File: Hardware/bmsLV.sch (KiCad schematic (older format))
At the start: 30 parts, among them J1 Conn_01x06_Male, J2 USB_B_Mini, K1 RM85V7, Q1 BSS138, SW1 SW_Push, U1 STM32F103C8Tx, Y1 Crystal

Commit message: Going back to work
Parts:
- added D16: D_Small, Diode_SMD:D_SMB, symbol Device:D_Small
- added J13: Conn_01x04_Male, Connector_PinHeader_2.54mm:PinHeader_1x04_P2.54mm_Vertical, symbol Connector:Conn_01x04_Male
- added R39, R40: 27, Resistor_SMD:R_1206_3216Metric, symbol Device:R_Small
- K1: footprint RM85V7:RM85V7-Z-24VDC -> RM85V7:RM85V7
- R1, R2, R3, R4: value 1K -> 120
- gave numbers to parts that had none: 2
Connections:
- net +24V: now also D16.1 (K)
- net +5V: now also J13.1 (Pin_1)
- net GND: now also J13.4 (Pin_4)
- net USB_DM: now also J13.2 (Pin_2), R39.1; no longer U1.32 (PA11)
- net USB_DP: now also J13.3 (Pin_3), R40.1; no longer U1.33 (PA12)
- net at K1.2 (A2), Q1.3 (D): now also D16.2 (A)
- new net: R39.2, U1.32 (PA11)
- new net: R40.2, U1.33 (PA12)
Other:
- moved on the sheet: J2
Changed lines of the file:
@@
 P 3400 4250
 F 0 "R2" V 3204 4250 50  0000 C CNN
-F 1 "1K" V 3295 4250 50  0000 C CNN
+F 1 "120" V 3295 4250 50  0000 C CNN
 F 2 "Resistor_SMD:R_1206_3216Metric" H 3400 4250 50  0001 C CNN
 F 3 "~" H 3400 4250 50  0001 C CNN
@@
 P 3400 5050
 F 0 "R3" V 3204 5050 50  0000 C CNN
-F 1 "1K" V 3295 5050 50  0000 C CNN
+F 1 "120" V 3295 5050 50  0000 C CNN
 F 2 "Resistor_SMD:R_1206_3216Metric" H 3400 5050 50  0001 C CNN
 F 3 "~" H 3400 5050 50  0001 C CNN
@@
 P 3400 5150
 F 0 "R4" V 3204 5150 50  0000 C CNN
-F 1 "1K" V 3295 5150 50  0000 C CNN
+F 1 "120" V 3295 5150 50  0000 C CNN
 F 2 "Resistor_SMD:R_1206_3216Metric" H 3400 5150 50  0001 C CNN
 F 3 "~" H 3400 5150 50  0001 C CNN
@@
 P 3400 4150
 F 0 "R1" V 3204 4150 50  0000 C CNN
-F 1 "1K" V 3295 4150 50  0000 C CNN
+F 1 "120" V 3295 4150 50  0000 C CNN
 F 2 "Resistor_SMD:R_1206_3216Metric" H 3400 4150 50  0001 C CNN
 F 3 "~" H 3400 4150 50  0001 C CNN
@@
 Wire Wire Line
 	3300 4250 3050 4250
-Text GLabel 5500 5250 2    50   Input ~ 0
+Text GLabel 6100 5250 2    50   Input ~ 0
 USB_DP
-Text GLabel 5500 5150 2    50   Input ~ 0
+Text GLabel 6100 5150 2    50   Input ~ 0
 USB_DM
 $Comp
 L Connector:USB_B_Mini J2
 U 1 1 5FFA0FD0
-P 8150 1550
-F 0 "J2" H 7920 1447 50  0000 R CNN
-F 1 "USB_B_Mini" H 7920 1538 50  0000 R CNN
-F 2 "Connector_USB:USB_Micro-B_Molex_47346-0001" H 8300 1500 50  0001 C CNN
-F 3 "~" H 8300 1500 50  0001 C CNN
-	1    8150 1550
+P 8450 1550
+F 0 "J2" H 8220 1447 50  0000 R CNN
+F 1 "USB_B_Mini" H 8220 1538 50  0000 R CNN
+F 2 "Connector_USB:USB_Micro-B_Molex_47346-0001" H 8600 1500 50  0001 C CNN
+F 3 "~" H 8600 1500 50  0001 C CNN
+	1    8450 1550
 	-1   0    0    1
 $EndComp
@@
 L power:GND #PWR019
 U 1 1 5FFA2879
-P 8450 1100
-F 0 "#PWR019" H 8450 850 50  0001 C CNN
-F 1 "GND" H 8455 927 50  0000 C CNN
-F 2 "" H 8450 1100 50  0001 C CNN
-F 3 "" H 8450 1100 50  0001 C CNN
-	1    8450 1100
-	1    0    0    -1
-$EndComp
-Wire Wire Line
-	8150 1100 8150 1150
+P 8750 1100
+F 0 "#PWR019" H 8750 850 50  0001 C CNN
+F 1 "GND" H 8755 927 50  0000 C CNN
+F 2 "" H 8750 1100 50  0001 C CNN
+F 3 "" H 8750 1100 50  0001 C CNN
+	1    8750 1100
+	1    0    0    -1
+$EndComp
+Wire Wire Line
+	8450 1100 8450 1150
 $Comp
 L power:+5V #PWR014
 U 1 1 5FFAAF0D
-P 7450 1750
-F 0 "#PWR014" H 7450 1600 50  0001 C CNN
-F 1 "+5V" H 7465 1923 50  0000 C CNN
-F 2 "" H 7450 1750 50  0001 C CNN
-F 3 "" H 7450 1750 50  0001 C CNN
-	1    7450 1750
-	1    0    0    -1
-$EndComp
-Wire Wire Line
-	8150 1100 8250 1100
-Wire Wire Line
-	8250 1150 8250 1100
-Connection ~ 8250 1100
-Wire Wire Line
-	8250 1100 8450 1100
-Text GLabel 7850 1450 0    50   Input ~ 0
+P 7750 1750
+F 0 "#PWR014" H 7750 1600 50  0001 C CNN
+F 1 "+5V" H 7765 1923 50  0000 C CNN
+F 2 "" H 7750 1750 50  0001 C CNN
+F 3 "" H 7750 1750 50  0001 C CNN
+	1    7750 1750
+	1    0    0    -1
+$EndComp
+Wire Wire Line
+	8450 1100 8550 1100
+Wire Wire Line
+	8550 1150 8550 1100
+Connection ~ 8550 1100
+Wire Wire Line
+	8550 1100 8750 1100
+Text GLabel 8150 1450 0    50   Input ~ 0
 USB_DM
-Text GLabel 7850 1550 0    50   Input ~ 0
+Text GLabel 8150 1550 0    50   Input ~ 0
 USB_DP
 Wire Wire Line
-	7450 1750 7850 1750
+	7750 1750 8150 1750
 $Comp
 L power:+3.3V #PWR03
@@
 P 7900 2450
 AR Path="/5FAD7AC5/5FFFFAC2" Ref="J?"  Part="1"
-AR Path="/5FFFFAC2" Ref="J?"  Part="1"
-F 0 "J?" H 7792 2125 50  0000 C CNN
+AR Path="/5FFFFAC2" Ref="J3"  Part="1"
+F 0 "J3" H 7792 2125 50  0000 C CNN
 F 1 "Conn_01x02_Female" H 7792 2216 50  0000 C CNN
 F 2 "TerminalBlock:TerminalBlock_bornier-2_P5.08mm" H 7900 2450 50  0001 C CNN
@@
 P 8250 2450
 AR Path="/5FAD7AC5/5FFFFAC8" Ref="#PWR?"  Part="1"
-AR Path="/5FFFFAC8" Ref="#PWR?"  Part="1"
-F 0 "#PWR?" H 8250 2200 50  0001 C CNN
+AR Path="/5FFFFAC8" Ref="#PWR0101"  Part="1"
+F 0 "#PWR0101" H 8250 2200 50  0001 C CNN
 F 1 "GND" H 8255 2277 50  0000 C CNN
 F 2 "" H 8250 2450 50  0001 C CNN
@@
 	8250 2350 8250 2300
 $Comp
-L power:VCC #PWR?
+L power:VCC #PWR0102
 U 1 1 60004D86
 P 8250 2300
-F 0 "#PWR?" H 8250 2150 50  0001 C CNN
+F 0 "#PWR0102" H 8250 2150 50  0001 C CNN
 F 1 "VCC" H 8267 2473 50  0000 C CNN
 F 2 "" H 8250 2300 50  0001 C CNN
@@
 P 7900 3000
 AR Path="/5FB83FF2/60009E9A" Ref="J?"  Part="1"
-AR Path="/60009E9A" Ref="J?"  Part="1"
-F 0 "J?" H 7928 2976 50  0000 L CNN
+AR Path="/60009E9A" Ref="J5"  Part="1"
+F 0 "J5" H 7928 2976 50  0000 L CNN
 F 1 "Conn_01x02_Female" H 7928 2885 50  0000 L CNN
 F 2 "TerminalBlock:TerminalBlock_bornier-2_P5.08mm" H 7900 3000 50  0001 C CNN
@@
 F 0 "K1" H 8375 5475 50  0000 C CNN
 F 1 "RM85V7" H 8375 5384 50  0000 C CNN
-F 2 "RM85V7:RM85V7-Z-24VDC" V 8500 5200 50  0001 C CNN
+F 2 "RM85V7:RM85V7" V 8500 5200 50  0001 C CNN
 F 3 "" V 8500 5200 50  0001 C CNN
 	1    8350 5200
@@
 Wire Wire Line
 	8000 5350 8000 5600
+$Comp
+L power:GND #PWR018
+U 1 1 6065B29C
+P 8000 6100
+F 0 "#PWR018" H 8000 5850 50  0001 C CNN
+F 1 "GND" H 8005 5927 50  0000 C CNN
+F 2 "" H 8000 6100 50  0001 C CNN
+F 3 "" H 8000 6100 50  0001 C CNN
+	1    8000 6100
+	1    0    0    -1
+$EndComp
+Wire Wire Line
+	7700 5800 7550 5800
+Wire Wire Line
+	7550 5800 7550 6050
+Wire Wire Line
+	7550 6050 7650 6050
+$Comp
+L Device:R_Small R8
+U 1 1 6065E7D3
+P 7750 6050
+F 0 "R8" V 7554 6050 50  0000 C CNN
+F 1 "10K" V 7645 6050 50  0000 C CNN
+F 2 "Resistor_SMD:R_1206_3216Metric" H 7750 6050 50  0001 C CNN
+F 3 "~" H 7750 6050 50  0001 C CNN
+	1    7750 6050
+	0    1    1    0
+$EndComp
+Wire Wire Line
+	8000 6000 8000 6050
+Wire Wire Line
+	8000 6050 7850 6050
+Connection ~ 8000 6050
+Wire Wire Line
+	8000 6050 8000 6100
+Wire Wire Line
+	7550 5800 7450 5800
+Connection ~ 7550 5800
+$Comp
+L Device:R_Small R7
+U 1 1 6066752D
+P 7350 5800
+F 0 "R7" V 7154 5800 50  0000 C CNN
+F 1 "100" V 7245 5800 50  0000 C CNN
+F 2 "Resistor_SMD:R_1206_3216Metric" H 7350 5800 50  0001 C CNN
+F 3 "~" H 7350 5800 50  0001 C CNN
+	1    7350 5800
+	0    1    1    0
+$EndComp
+Wire Wire Line
+	7250 5800 7150 5800
+Wire Wire Line
+	8750 5200 8850 5200
+Wire Wire Line
+	8750 5300 8850 5300
+Text GLabel 8850 5300 2    50   Input ~ 0
+V_Out
+$Comp
+L power:+24V #PWR020
+U 1 1 6068138D
+P 8850 5200
+F 0 "#PWR020" H 8850 5050 50  0001 C CNN
+F 1 "+24V" V 8865 5328 50  0000 L CNN
+F 2 "" H 8850 5200 50  0001 C CNN
+F 3 "" H 8850 5200 50  0001 C CNN
+	1    8850 5200
+	1    0    0    -1
+$EndComp
+Wire Wire Line
+	8000 5350 7900 5350
+Wire Wire Line
+	7900 5150 8000 5150
+Connection ~ 8000 5350
+Connection ~ 8000 5150
+$Comp
+L Device:D_Small D16
+U 1 1 60308393
+P 7900 5250
+F 0 "D16" H 7900 5455 50  0000 C CNN
+F 1 "D_Small" H 7900 5364 50  0000 C CNN
+F 2 "Diode_SMD:D_SMB" V 7900 5250 50  0001 C CNN
+F 3 "~" V 7900 5250 50  0001 C CNN
+	1    7900 5250
+	0    1    1    0
+$EndComp
 $Comp
 L Transistor_FET:BSS138 Q1
@@
 $EndComp
 $Comp
-L power:GND #PWR018
-U 1 1 6065B29C
-P 8000 6100
-F 0 "#PWR018" H 8000 5850 50  0001 C CNN
-F 1 "GND" H 8005 5927 50  0000 C CNN
-F 2 "" H 8000 6100 50  0001 C CNN
-F 3 "" H 8000 6100 50  0001 C CNN
-	1    8000 6100
-	1    0    0    -1
-$EndComp
-Wire Wire Line
-	7700 5800 7550 5800
-Wire Wire Line
-	7550 5800 7550 6050
-Wire Wire Line
-	7550 6050 7650 6050
-$Comp
-L Device:R_Small R8
-U 1 1 6065E7D3
-P 7750 6050
-F 0 "R8" V 7554 6050 50  0000 C CNN
-F 1 "10K" V 7645 6050 50  0000 C CNN
-F 2 "Resistor_SMD:R_1206_3216Metric" H 7750 6050 50  0001 C CNN
-F 3 "~" H 7750 6050 50  0001 C CNN
-	1    7750 6050
-	0    1    1    0
-$EndComp
-Wire Wire Line
-	8000 6000 8000 6050
-Wire Wire Line
-	8000 6050 7850 6050
-Connection ~ 8000 6050
-Wire Wire Line
-	8000 6050 8000 6100
-Wire Wire Line
-	7550 5800 7450 5800
-Connection ~ 7550 5800
-$Comp
-L Device:R_Small R7
-U 1 1 6066752D
-P 7350 5800
-F 0 "R7" V 7154 5800 50  0000 C CNN
-F 1 "100" V 7245 5800 50  0000 C CNN
-F 2 "Resistor_SMD:R_1206_3216Metric" H 7350 5800 50  0001 C CNN
-F 3 "~" H 7350 5800 50  0001 C CNN
-	1    7350 5800
-	0    1    1    0
-$EndComp
-Wire Wire Line
-	7250 5800 7150 5800
-Wire Wire Line
-	8750 5200 8850 5200
-Wire Wire Line
-	8750 5300 8850 5300
-Text GLabel 8850 5300 2    50   Input ~ 0
-V_Out
-$Comp
-L power:+24V #PWR020
-U 1 1 6068138D
-P 8850 5200
-F 0 "#PWR020" H 8850 5050 50  0001 C CNN
-F 1 "+24V" V 8865 5328 50  0000 L CNN
-F 2 "" H 8850 5200 50  0001 C CNN
-F 3 "" H 8850 5200 50  0001 C CNN
-	1    8850 5200
-	1    0    0    -1
-$EndComp
+L Connector:Conn_01x04_Male J13
+U 1 1 60342BDE
+P 7000 1450
+F 0 "J13" H 7108 1731 50  0000 C CNN
+F 1 "Conn_01x04_Male" H 7108 1640 50  0000 C CNN
+F 2 "Connector_PinHeader_2.54mm:PinHeader_1x04_P2.54mm_Vertical" H 7000 1450 50  0001 C CNN
+F 3 "~" H 7000 1450 50  0001 C CNN
+	1    7000 1450
+	1    0    0    -1
+$EndComp
+$Comp
+L power:+5V #PWR0104
+U 1 1 6034A78E
+P 7200 1350
+F 0 "#PWR0104" H 7200 1200 50  0001 C CNN
+F 1 "+5V" H 7215 1523 50  0000 C CNN
+F 2 "" H 7200 1350 50  0001 C CNN
+F 3 "" H 7200 1350 50  0001 C CNN
+	1    7200 1350
+	1    0    0    -1
+$EndComp
+Text GLabel 7200 1450 2    50   Input ~ 0
+USB_DM
+Text GLabel 7200 1550 2    50   Input ~ 0
+USB_DP
+$Comp
+L power:GND #PWR0105
+U 1 1 60352852
+P 7200 1650
+F 0 "#PWR0105" H 7200 1400 50  0001 C CNN
+F 1 "GND" H 7205 1477 50  0000 C CNN
+F 2 "" H 7200 1650 50  0001 C CNN
+F 3 "" H 7200 1650 50  0001 C CNN
+	1    7200 1650
+	1    0    0    -1
+$EndComp
+$Comp
+L Device:R_Small R39
+U 1 1 6036F928
+P 5800 5150
+F 0 "R39" V 5604 5150 50  0000 C CNN
+F 1 "27" V 5695 5150 50  0000 C CNN
+F 2 "Resistor_SMD:R_1206_3216Metric" H 5800 5150 50  0001 C CNN
+F 3 "~" H 5800 5150 50  0001 C CNN
+	1    5800 5150
+	0    1    1    0
+$EndComp
+$Comp
+L Device:R_Small R40
+U 1 1 60370D0A
+P 5800 5250
+F 0 "R40" V 5604 5250 50  0000 C CNN
+F 1 "27" V 5695 5250 50  0000 C CNN
+F 2 "Resistor_SMD:R_1206_3216Metric" H 5800 5250 50  0001 C CNN
+F 3 "~" H 5800 5250 50  0001 C CNN
+	1    5800 5250
+	0    1    1    0
+$EndComp
+Wire Wire Line
+	5500 5150 5700 5150
+Wire Wire Line
+	5500 5250 5700 5250
+Wire Wire Line
+	5900 5150 6100 5150
+Wire Wire Line
+	5900 5250 6100 5250
 $EndSCHEMATC

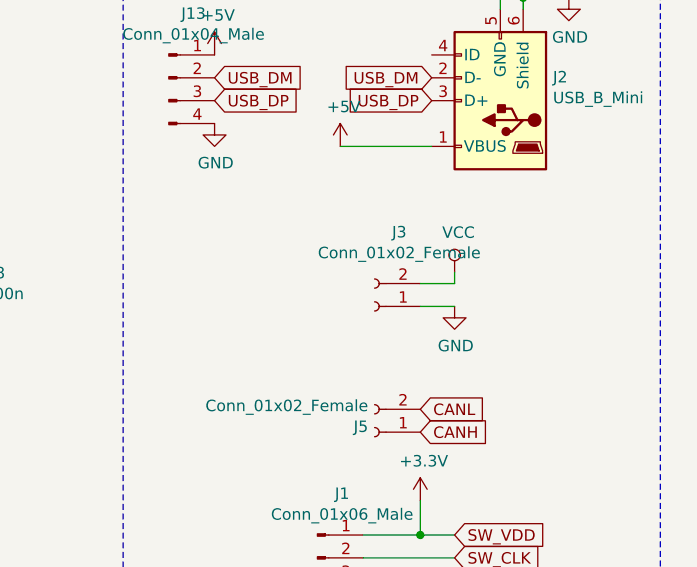
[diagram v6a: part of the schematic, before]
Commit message: PCB changes + MXCube
-gitignore added to the Hardware and Software sections
-Changed power section wiring on PCB
-MXCube file created as a beginning of Software section
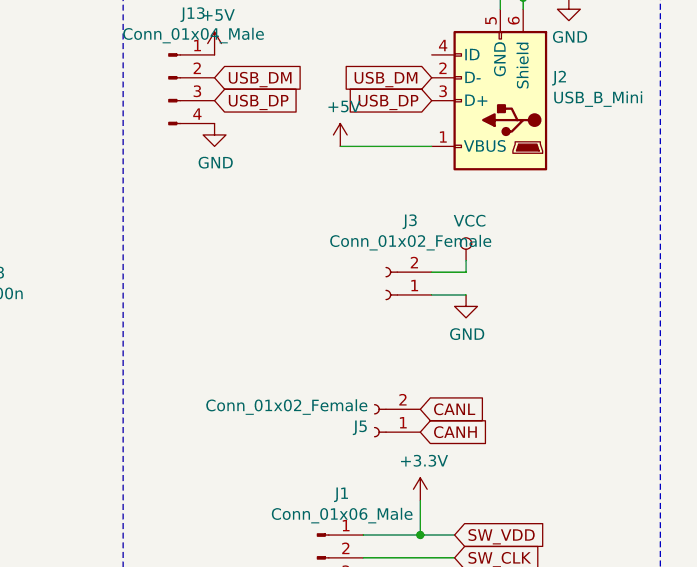
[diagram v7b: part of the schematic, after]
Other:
- moved on the sheet: J3
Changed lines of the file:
@@
 L Connector:Conn_01x02_Female J?
 U 1 1 5FFFFAC2
-P 7900 2450
+P 7950 2400
 AR Path="/5FAD7AC5/5FFFFAC2" Ref="J?"  Part="1"
 AR Path="/5FFFFAC2" Ref="J3"  Part="1"
-F 0 "J3" H 7792 2125 50  0000 C CNN
-F 1 "Conn_01x02_Female" H 7792 2216 50  0000 C CNN
-F 2 "TerminalBlock:TerminalBlock_bornier-2_P5.08mm" H 7900 2450 50  0001 C CNN
-F 3 "~" H 7900 2450 50  0001 C CNN
-	1    7900 2450
+F 0 "J3" H 7842 2075 50  0000 C CNN
+F 1 "Conn_01x02_Female" H 7842 2166 50  0000 C CNN
+F 2 "TerminalBlock:TerminalBlock_bornier-2_P5.08mm" H 7950 2400 50  0001 C CNN
+F 3 "~" H 7950 2400 50  0001 C CNN
+	1    7950 2400
 	-1   0    0    1
 $EndComp
@@
 L power:GND #PWR?
 U 1 1 5FFFFAC8
-P 8250 2450
+P 8300 2400
 AR Path="/5FAD7AC5/5FFFFAC8" Ref="#PWR?"  Part="1"
 AR Path="/5FFFFAC8" Ref="#PWR0101"  Part="1"
-F 0 "#PWR0101" H 8250 2200 50  0001 C CNN
-F 1 "GND" H 8255 2277 50  0000 C CNN
-F 2 "" H 8250 2450 50  0001 C CNN
-F 3 "" H 8250 2450 50  0001 C CNN
-	1    8250 2450
+F 0 "#PWR0101" H 8300 2150 50  0001 C CNN
+F 1 "GND" H 8305 2227 50  0000 C CNN
+F 2 "" H 8300 2400 50  0001 C CNN
+F 3 "" H 8300 2400 50  0001 C CNN
+	1    8300 2400
 	1    0    0    -1
 $EndComp
 Wire Wire Line
-	8250 2450 8100 2450
+	8300 2400 8150 2400
 Wire Wire Line
-	8100 2350 8250 2350
+	8150 2300 8300 2300
 Wire Wire Line
-	8250 2350 8250 2300
+	8300 2300 8300 2250
 $Comp
 L power:VCC #PWR0102
 U 1 1 60004D86
-P 8250 2300
-F 0 "#PWR0102" H 8250 2150 50  0001 C CNN
-F 1 "VCC" H 8267 2473 50  0000 C CNN
-F 2 "" H 8250 2300 50  0001 C CNN
-F 3 "" H 8250 2300 50  0001 C CNN
-	1    8250 2300
+P 8300 2250
+F 0 "#PWR0102" H 8300 2100 50  0001 C CNN
+F 1 "VCC" H 8317 2423 50  0000 C CNN
+F 2 "" H 8300 2250 50  0001 C CNN
+F 3 "" H 8300 2250 50  0001 C CNN
+	1    8300 2250
 	1    0    0    -1
 $EndComp
